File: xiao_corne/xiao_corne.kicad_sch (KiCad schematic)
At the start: 70 parts, among them SW1 SW_Push, SW10 SW_Push, SW11 SW_Push, SW12 SW_Push, SW13 SW_Push, SW17 SW_Push, SW18 SW_Push, SW19 SW_Push, SW2 SW_Push, SW20 SW_Push, SW21 SW_Push, SW22 SW_Push, SW23 SW_Push, SW24 SW_Push, SW25 SW_Push, SW26 SW_Push, SW27 SW_Push, SW3 SW_Push, SW4 SW_Push, SW5 SW_Push, SW9 SW_Push, U1 XIAO-ESP32-S3-SMD, U2 SN74AHCT125DR, U3 MCP1253-33X50I/MS

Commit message: Hardware V0.2
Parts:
- added BT2: Battery, ScottoKeebs_Scotto:Battery, symbol Device:Battery
- added C4, C5: 10uF, footprints_grm:G-21_MUR, symbol 2025-03-05_20-15-47:GRM21BR61C106KE15K
- added C6: 1uF, footprints_cl1:CAP_CL10_SAM, symbol 2025-03-05_20-11-15:CL10B105KA8NNNC
- added D43, D44, D45, D46, D47, D48, D49, D50, D51, D52, D53, D54, D55, D56, D57, D58, D59, D60, D61, D62, D63: D, ScottoKeebs_Components:Diode_SOD-123, symbol Device:D
- added D64, D65, D66, D67, D68, D69, D70, D71, D72, D73, D74, D75, D76, D77, D78, D79, D80, D81, D82, D83, D84: LED_SK6812MINI, ScottoKeebs_Components:LED_SK6812MINI, symbol ScottoKeebs:LED_SK6812MINI
- added J1, J2: Conn_01x04_Socket, Connector_PinHeader_2.54mm:PinHeader_1x04_P2.54mm_Vertical, symbol Connector:Conn_01x04_Socket
- added SW14, SW15, SW16, SW28, SW29, SW30, SW31, SW32, SW33, SW34, SW35, SW36, SW37, SW38, SW39, SW40, SW41, SW42, SW6, SW7, SW8: SW_Push, ScottoKeebs_Hotswap:Hotswap_Choc_V1V2_1.00u, symbol Switch:SW_Push
- added U4: XIAO-ESP32-S3-SMD, Seeed_Studio_XIAO_Series:XIAO-ESP32-S3-SMD, symbol Seeed_Studio_XIAO_Series-20240814:XIAO-ESP32-S3-SMD
- added U5: MCP1253-33X50I/MS, footprints_mcp:MSOP8_MC_MCH, symbol 2025-03-05_20-04-50:MCP1253-33X50I_MS
- added U6: SN74AHCT125DR, footprints_sn7:D14, symbol 2025-03-05_20-42-17:SN74AHCT125DR
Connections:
- net +5V: now also C4.1, D64.1 (VDD), D65.1 (VDD), D66.1 (VDD), D67.1 (VDD), D68.1 (VDD), D69.1 (VDD), D70.1 (VDD), D71.1 (VDD), D72.1 (VDD), D73.1 (VDD), D74.1 (VDD), D75.1 (VDD), D76.1 (VDD), D77.1 (VDD), D78.1 (VDD), D79.1 (VDD), D80.1 (VDD), D81.1 (VDD), D82.1 (VDD), D83.1 (VDD), D84.1 (VDD), U5.2 (VOUT), U6.14 (VCC); no longer C3.1, D14.1 (VDD), D15.1 (VDD), D16.1 (VDD), D28.1 (VDD), D29.1 (VDD), D30.1 (VDD), D31.1 (VDD), D32.1 (VDD), D33.1 (VDD), D34.1 (VDD), D35.1 (VDD), D36.1 (VDD), D37.1 (VDD), D38.1 (VDD), D39.1 (VDD), D40.1 (VDD), D41.1 (VDD), D42.1 (VDD), D6.1 (VDD), D7.1 (VDD), D8.1 (VDD), U2.14 (VCC), U3.2 (VOUT)
- net C1: now also D43.2 (A), D44.2 (A), D45.2 (A), D46.2 (A), D47.2 (A), U4.6 (PA9_A5_D5_SCL); no longer D1.2 (A), D17.2 (A), D22.2 (A), D27.2 (A), D9.2 (A), U1.6 (PA9_A5_D5_SCL)
- net C2: now also D48.2 (A), D49.2 (A), D50.2 (A), D51.2 (A), U4.7 (PB08_A6_D6_TX); no longer D10.2 (A), D18.2 (A), D2.2 (A), D23.2 (A), U1.7 (PB08_A6_D6_TX)
- net C3: now also D52.2 (A), D53.2 (A), D54.2 (A), D55.2 (A), U4.8 (PB09_A7_D7_RX); no longer D11.2 (A), D19.2 (A), D24.2 (A), D3.2 (A), U1.8 (PB09_A7_D7_RX)
- net C4: now also D56.2 (A), D57.2 (A), D58.2 (A), D59.2 (A), U4.9 (PA7_A8_D8_SCK); no longer D12.2 (A), D20.2 (A), D25.2 (A), D4.2 (A), U1.9 (PA7_A8_D8_SCK)
- net C5: now also D60.2 (A), D61.2 (A), D62.2 (A), D63.2 (A), U4.10 (PA5_A9_D9_MISO); no longer D13.2 (A), D21.2 (A), D26.2 (A), D5.2 (A), U1.10 (PA5_A9_D9_MISO)
- net GND: now also BT2.2 (-), C4.2, C5.2, D64.3 (VSS), D65.3 (VSS), D66.3 (VSS), D67.3 (VSS), D68.3 (VSS), D69.3 (VSS), D70.3 (VSS), D71.3 (VSS), D72.3 (VSS), D73.3 (VSS), D74.3 (VSS), D75.3 (VSS), D76.3 (VSS), D77.3 (VSS), D78.3 (VSS), D79.3 (VSS), D80.3 (VSS), D81.3 (VSS), D82.3 (VSS), D83.3 (VSS), D84.3 (VSS), J2.4 (Pin_4), U4.13 (GND), U4.16 (GND), U4.20 (GND), U5.4 (GND), U5.8 (SELECT), U6.1 (*1OE), U6.7 (GND); no longer BT1.2 (-), C2.2, C3.2, D14.3 (VSS), D15.3 (VSS), D16.3 (VSS), D28.3 (VSS), D29.3 (VSS), D30.3 (VSS), D31.3 (VSS), D32.3 (VSS), D33.3 (VSS), D34.3 (VSS), D35.3 (VSS), D36.3 (VSS), D37.3 (VSS), D38.3 (VSS), D39.3 (VSS), D40.3 (VSS), D41.3 (VSS), D42.3 (VSS), D6.3 (VSS), D7.3 (VSS), D8.3 (VSS), U1.13 (GND), U1.16 (GND), U1.20 (GND), U2.1 (*1OE), U2.7 (GND), U3.4 (GND), U3.8 (SELECT)
- net LED_3v: now also U4.11 (PA6_A10_D10_MOSI), U6.2 (1A); no longer U1.11 (PA6_A10_D10_MOSI), U2.2 (1A)
- net LED_5v: now also D64.4 (DIN), U6.3 (1Y); no longer D6.4 (DIN), U2.3 (1Y)
- net R1: now also SW35.2, SW39.2, SW6.2, SW7.2, SW8.2, U4.1 (PA02_A0_D0); no longer SW1.2, SW2.2, SW3.2, SW4.2, SW5.2, U1.1 (PA02_A0_D0)
- net R2: now also SW14.2, SW15.2, SW16.2, SW36.2, SW40.2, U4.2 (PA4_A1_D1); no longer SW10.2, SW11.2, SW12.2, SW13.2, SW9.2, U1.2 (PA4_A1_D1)
- net R3: now also SW28.2, SW31.2, SW33.2, SW37.2, SW41.2, U4.3 (PA10_A2_D2); no longer SW17.2, SW18.2, SW19.2, SW20.2, SW21.2, U1.3 (PA10_A2_D2)
- net R4: now also SW29.2, SW32.2, SW34.2, SW38.2, SW42.2, U4.4 (PA11_A3_D3); no longer SW22.2, SW23.2, SW24.2, SW25.2, SW26.2, U1.4 (PA11_A3_D3)
- net R5: now also SW30.2, U4.5 (PA8_A4_D4_SDA); no longer SW27.2, U1.5 (PA8_A4_D4_SDA)
- net +5V L USB: now reaches U1.14 (5V)
- net +5V L USB: now also J1.1 (Pin_1)
- new net: D60.1 (K), SW39.1
- new net: D66.4 (DIN), D84.2 (DOUT)
- new net: D82.2 (DOUT), D84.4 (DIN)
- new net: C5.1, U4.12 (3V3), U5.3 (VIN), U5.7 (*SHDN)
- new net: C6.1, U5.6 (C+)
- new net: C6.2, U5.5 (C-)
- new net: D50.1 (K), SW31.1
- new net: D59.1 (K), SW38.1
- new net: BT2.1 (+), U4.15 (BAT)
- new net: D46.1 (K), SW29.1
- new net: D75.2 (DOUT), D78.4 (DIN)
- new net: D43.1 (K), SW6.1
- new net: D53.1 (K), SW16.1
- new net: D63.1 (K), SW42.1
- new net: D48.1 (K), SW7.1
- new net: D62.1 (K), SW41.1
- new net: D66.2 (DOUT), D69.4 (DIN)
- new net: D61.1 (K), SW40.1
- new net: D76.2 (DOUT), D79.4 (DIN)
- new net: D73.2 (DOUT), D76.4 (DIN)
- new net: D49.1 (K), SW15.1
- new net: D80.2 (DOUT), D82.4 (DIN)
- new net: D77.2 (DOUT), D80.4 (DIN)
- new net: D51.1 (K), SW32.1
- new net: D54.1 (K), SW33.1
- new net: D79.2 (DOUT), D81.4 (DIN)
- new net: D68.2 (DOUT), D71.4 (DIN)
- new net: D65.2 (DOUT), D68.4 (DIN)
- new net: D56.1 (K), SW35.1
- new net: D45.1 (K), SW28.1
- new net: D44.1 (K), SW14.1
- new net: D65.4 (DIN), D83.2 (DOUT)
- new net: D71.2 (DOUT), D74.4 (DIN)
- new net: D69.2 (DOUT), D72.4 (DIN)
- new net: D52.1 (K), SW8.1
- new net: D64.2 (DOUT), D67.4 (DIN)
- new net: D74.2 (DOUT), D77.4 (DIN)
- new net: D47.1 (K), SW30.1
- new net: D55.1 (K), SW34.1
- new net: D67.2 (DOUT), D70.4 (DIN)
- new net: D70.2 (DOUT), D73.4 (DIN)
- new net: D81.2 (DOUT), D83.4 (DIN)
- new net: D57.1 (K), SW36.1
- new net: D72.2 (DOUT), D75.4 (DIN)
- new net: D58.1 (K), SW37.1
- new net +5V L: C3.1, D14.1 (VDD), D15.1 (VDD), D16.1 (VDD), D28.1 (VDD), D29.1 (VDD), D30.1 (VDD), D31.1 (VDD), D32.1 (VDD), D33.1 (VDD), D34.1 (VDD), D35.1 (VDD), D36.1 (VDD), D37.1 (VDD), D38.1 (VDD), D39.1 (VDD), D40.1 (VDD), D41.1 (VDD), D42.1 (VDD), D6.1 (VDD), D7.1 (VDD), D8.1 (VDD), U2.14 (VCC), U3.2 (VOUT)
- new net +5V USB: J2.1 (Pin_1), U4.14 (5V)
- new net C1 L: D1.2 (A), D17.2 (A), D22.2 (A), D27.2 (A), D9.2 (A), U1.6 (PA9_A5_D5_SCL)
- new net C2 L: D10.2 (A), D18.2 (A), D2.2 (A), D23.2 (A), U1.7 (PB08_A6_D6_TX)
- new net C3 L: D11.2 (A), D19.2 (A), D24.2 (A), D3.2 (A), U1.8 (PB09_A7_D7_RX)
- new net C4 L: D12.2 (A), D20.2 (A), D25.2 (A), D4.2 (A), U1.9 (PA7_A8_D8_SCK)
- new net C5 L: D13.2 (A), D21.2 (A), D26.2 (A), D5.2 (A), U1.10 (PA5_A9_D9_MISO)
- new net GND L: BT1.2 (-), C2.2, C3.2, D14.3 (VSS), D15.3 (VSS), D16.3 (VSS), D28.3 (VSS), D29.3 (VSS), D30.3 (VSS), D31.3 (VSS), D32.3 (VSS), D33.3 (VSS), D34.3 (VSS), D35.3 (VSS), D36.3 (VSS), D37.3 (VSS), D38.3 (VSS), D39.3 (VSS), D40.3 (VSS), D41.3 (VSS), D42.3 (VSS), D6.3 (VSS), D7.3 (VSS), D8.3 (VSS), J1.4 (Pin_4), U1.13 (GND), U1.16 (GND), U1.20 (GND), U2.1 (*1OE), U2.7 (GND), U3.4 (GND), U3.8 (SELECT)
- new net LED_3v L: U1.11 (PA6_A10_D10_MOSI), U2.2 (1A)
- new net LED_5v L: D6.4 (DIN), U2.3 (1Y)
- new net R1 L: SW1.2, SW2.2, SW3.2, SW4.2, SW5.2, U1.1 (PA02_A0_D0)
- new net R2 L: SW10.2, SW11.2, SW12.2, SW13.2, SW9.2, U1.2 (PA4_A1_D1)
- new net R3 L: SW17.2, SW18.2, SW19.2, SW20.2, SW21.2, U1.3 (PA10_A2_D2)
- new net R4 L: SW22.2, SW23.2, SW24.2, SW25.2, SW26.2, U1.4 (PA11_A3_D3)
- new net R5 L: SW27.2, U1.5 (PA8_A4_D4_SDA)
- no-connect marks 18 -> 40

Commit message: Major work for update to 0.3!
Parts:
- removed C1, C6: 1uF, footprints_cl1:CAP_CL10_SAM, symbol 2025-03-05_20-11-15:CL10B105KA8NNNC
- removed C2, C3, C4, C5: 10uF, footprints_grm:G-21_MUR, symbol 2025-03-05_20-15-47:GRM21BR61C106KE15K
- removed U1, U4: XIAO-ESP32-S3-SMD, Seeed_Studio_XIAO_Series:XIAO-ESP32-S3-SMD, symbol Seeed_Studio_XIAO_Series-20240814:XIAO-ESP32-S3-SMD
- removed U3, U5: MCP1253-33X50I/MS, footprints_mcp:MSOP8_MC_MCH, symbol 2025-03-05_20-04-50:MCP1253-33X50I_MS
- added C1, C2, C3, C4, C5, C7: 10uF, Capacitor_SMD:C_0805_2012Metric, symbol Device:C
- added C10, C9: 100nF, Capacitor_SMD:C_0805_2012Metric, symbol Device:C
- added C6, C8: 1uF, Capacitor_SMD:C_0603_1608Metric, symbol Device:C
- added D78, D79, D80, D86, D87, D88: LED_SK6812MINI, ScottoKeebs_Components:LED_SK6812MINI, symbol ScottoKeebs:LED_SK6812MINI
- added J10, J2, J3, J4, J5, J7, J8, J9: Conn_01x04_Socket, Connector_PinHeader_2.54mm:PinHeader_1x04_P2.54mm_Vertical, symbol Connector:Conn_01x04_Socket
- added L1, L2: 2.2uH, Inductor_SMD:L_0805_2012Metric, symbol Device:L
- added R1, R2, R3, R4: 100k, Resistor_SMD:R_0805_2012Metric, symbol Device:R
- added S1, S2: SLW-864574-5A-RA-N-D, KiCad:SLW8645745ARAND, symbol SLW-864574-5A-RA-N-D:SLW-864574-5A-RA-N-D
- added U3, U4: XIAO-HALF-HOLE-23P, xiao ESP32S3 Plus_PCB:MOUDLE23P-SMD-2.54-21X17.8MM.kicad_mod.kicad_sym, symbol MOUDLE-SEEEDUINO-XIAO-ESP32S3-Plus:Module/XIAO-HALF-HOLE-23P
- added U5, U6: TPS61202DRCR, TPS61202DRCR:VREG_V62_16624-01YE, symbol TPS61202DRCR:TPS61202DRCR
- renumbered D60 to D10, D9 to D11, D10 to D12, D11 to D13, D12 to D14, D13 to D15, D6 to D16, D7 to D17, D8 to D18, D14 to D19, D15 to D20, D16 to D21, D28 to D22, D29 to D23, D44 to D24, D49 to D25, D53 to D26, D57 to D27, D61 to D28, D64 to D29, D67 to D30, D70 to D31, D73 to D32, D76 to D33, D79 to D34, D81 to D35, D83 to D36, D17 to D37, D18 to D38, D19 to D39, D20 to D40, D21 to D41, D45 to D42, D50 to D43, D54 to D44, D58 to D45, D62 to D46, D30 to D47, D31 to D48, D32 to D49, D33 to D50, D34 to D51, D35 to D52, D36 to D53, D37 to D54, D65 to D55, D68 to D56, D71 to D57, D74 to D58, D77 to D59, D43 to D6, D80 to D60, D82 to D61, D84 to D62, D22 to D63, D23 to D64, D24 to D65, D25 to D66, D26 to D67, D46 to D68, D51 to D69, D48 to D7, D55 to D70, D59 to D71, D63 to D72, D38 to D73, D39 to D74, D40 to D75, D41 to D76, D42 to D77, D52 to D8, D66 to D81, D69 to D82, D72 to D83, D75 to D84, D78 to D85, D27 to D89, D56 to D9, D47 to D90, J2 to J1, J1 to J6, SW39 to SW10, SW9 to SW11, SW10 to SW12, SW11 to SW13, SW12 to SW14, SW13 to SW15, SW14 to SW16, SW15 to SW17, SW16 to SW18, SW36 to SW19, SW40 to SW20, SW17 to SW21, SW18 to SW22, SW19 to SW23, SW20 to SW24, SW21 to SW25, SW28 to SW26, SW31 to SW27, SW33 to SW28, SW37 to SW29, SW41 to SW30, SW22 to SW31, SW23 to SW32, SW24 to SW33, SW25 to SW34, SW26 to SW35, SW29 to SW36, SW32 to SW37, SW34 to SW38, SW38 to SW39, SW42 to SW40, SW27 to SW41, SW30 to SW42, SW35 to SW9, U2 to U1, U6 to U2
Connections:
- net +5V: now also C3.2, C4.2, D86.1 (VDD), D87.1 (VDD), D88.1 (VDD), J2.1 (Pin_1), J3.1 (Pin_1), U6.10 (FB), U6.2 (VOUT)
- net +5V L: now also C1.2, C2.2, D78.1 (VDD), D79.1 (VDD), D80.1 (VDD), J4.1 (Pin_1), J5.1 (Pin_1), U5.10 (FB), U5.2 (VOUT)
- net +5V L USB: now also U3.14 (VBUS)
- net +5V USB: now also U4.14 (VBUS)
- net C1: now also U4.6 (GPIO6_D5/A5/I2C_SCL)
- net C1 L: now also U3.6 (GPIO6_D5/A5/I2C_SCL)
- net C2: now also U4.7 (U0TXD_D6/TX)
- net C2 L: now also U3.7 (U0TXD_D6/TX)
- net C3: now also U4.8 (U0RXD_D7/RX)
- net C3 L: now also U3.8 (U0RXD_D7/RX)
- net C4: now also U4.9 (GPIO7_D8/A8/SCK)
- net C4 L: now also U3.9 (GPIO7_D8/A8/SCK)
- net C5: now also U4.10 (GPIO8_D9/A9/MISO)
- net C5 L: now also U3.10 (GPIO8_D9/A9/MISO)
- net GND: now also C10.1, C3.1, C4.1, C7.1, C8.1, D86.3 (VSS), D87.3 (VSS), D88.3 (VSS), J2.4 (Pin_4), J3.4 (Pin_4), J7.4 (Pin_4), J8.4 (Pin_4), U4.13 (GND), U4.26 (GND), U4.32 (BAT-), U6.4 (PGND), U6.9 (GND)
- net GND L: now also C1.1, C2.1, C5.1, C6.1, C9.1, D78.3 (VSS), D79.3 (VSS), D80.3 (VSS), J10.4 (Pin_4), J4.4 (Pin_4), J5.4 (Pin_4), J9.4 (Pin_4), U3.13 (GND), U3.26 (GND), U3.32 (BAT-), U5.4 (PGND), U5.9 (GND)
- net LED_3v: now also U4.11 (GPIO9_D10/A10/MOSI)
- net LED_3v L: now also U3.11 (GPIO9_D10/A10/MOSI)
- net R1: now also U4.1 (GPIO1_D0/A0)
- net R1 L: now also U3.1 (GPIO1_D0/A0)
- net R2: now also U4.2 (GPIO2_D1/A1)
- net R2 L: now also U3.2 (GPIO2_D1/A1)
- net R3: now also U4.3 (GPIO3_D2/A2)
- net R3 L: now also U3.3 (GPIO3_D2/A2)
- net R4: now also U4.4 (GPIO4_D3/A3)
- net R4 L: now also U3.4 (GPIO4_D3/A3)
- net R5: now also U4.5 (GPIO5_D4/A4/I2C_SDA)
- net R5 L: now also U3.5 (GPIO5_D4/A4/I2C_SDA)
- net at BT2.1 (+): now also S2.3
- net at D85.2 (DOUT): now also D86.4 (DIN)
- net at D77.2 (DOUT): now also D78.4 (DIN)
- net at BT1.1 (+): now also S1.3
- new net: R1.2, U3.20 (GPIO10_XMCLK/ADC_BAT)
- new net: R3.2, S1.2, U3.33 (BAT+)
- new net: C6.2, U5.1 (VAUX)
- new net: R4.2, S2.2, U4.33 (BAT+)
- new net: C9.2, R1.1, R3.1
- new net: L1.1, U5.3 (L)
- new net: D87.2 (DOUT), D88.4 (DIN)
- new net: D79.2 (DOUT), D80.4 (DIN)
- new net: L2.1, U6.3 (L)
- new net: D86.2 (DOUT), D87.4 (DIN)
- new net: D78.2 (DOUT), D79.4 (DIN)
- new net: C10.2, R2.1, R4.1
- new net: R2.2, U4.20 (GPIO10_XMCLK/ADC_BAT)
- new net +3.3V: C7.2, C8.2, J7.1 (Pin_1), J8.1 (Pin_1), L2.2, U4.12 (VCC_3V3), U6.1 (VAUX), U6.5 (VIN), U6.6 (EN), U6.7 (UVLO), U6.8 (PS)
- new net +3.3V L: C5.2, J10.1 (Pin_1), J9.1 (Pin_1), L1.2, U3.12 (VCC_3V3), U5.5 (VIN), U5.6 (EN), U5.7 (UVLO), U5.8 (PS)
- new net GPIO_1: J2.2 (Pin_2), U4.15 (GPIO38_DVP_VSYNC/I2S_SD)
- new net GPIO_1_L: J4.2 (Pin_2), U3.15 (GPIO38_DVP_VSYNC/I2S_SD)
- new net GPIO_2: J2.3 (Pin_3), U4.16 (GPIO39_CAM_SCL/I2S_SCK)
- new net GPIO_2_L: J4.3 (Pin_3), U3.16 (GPIO39_CAM_SCL/I2S_SCK)
- new net GPIO_3: J7.2 (Pin_2), U4.17 (GPIO40_CAM_SDA/I2S_WS)
- new net GPIO_3_L: J9.2 (Pin_2), U3.17 (GPIO40_CAM_SDA/I2S_WS)
- new net GPIO_4: J7.3 (Pin_3), U4.18 (GPIO41_PDM_DATA/RX1)
- new net GPIO_4_L: J9.3 (Pin_3), U3.18 (GPIO41_PDM_DATA/RX1)
- new net GPIO_5: J3.2 (Pin_2), U4.19 (GPIO42_PDM_CLK/TX1)
- new net GPIO_5_L: J5.2 (Pin_2), U3.19 (GPIO42_PDM_CLK/TX1)
- new net GPIO_6: J3.3 (Pin_3), U4.21 (GPIO11_DVP_Y8/SPI_MOSI1)
- new net GPIO_6_L: J5.3 (Pin_3), U3.21 (GPIO11_DVP_Y8/SPI_MOSI1)
- new net GPIO_7: J8.2 (Pin_2), U4.22 (GPIO12_DVP_Y7/SPI_MISO1)
- new net GPIO_7_L: J10.2 (Pin_2), U3.22 (GPIO12_DVP_Y7/SPI_MISO1)
- new net GPIO_8: J8.3 (Pin_3), U4.23 (GPIO13_DVP_PCLK/SPI_SCK1)
- new net GPIO_8_L: J10.3 (Pin_3), U3.23 (GPIO13_DVP_PCLK/SPI_SCK1)
- no-connect marks 40 -> 46
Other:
- note added: "Done (v0.2 - v0.3): Add new LEDs Change voltage converter Switch to esp32c3 plus Add battery voltage sense line Expansion board GPIO Add switch for battery"
- moved on the sheet: J1

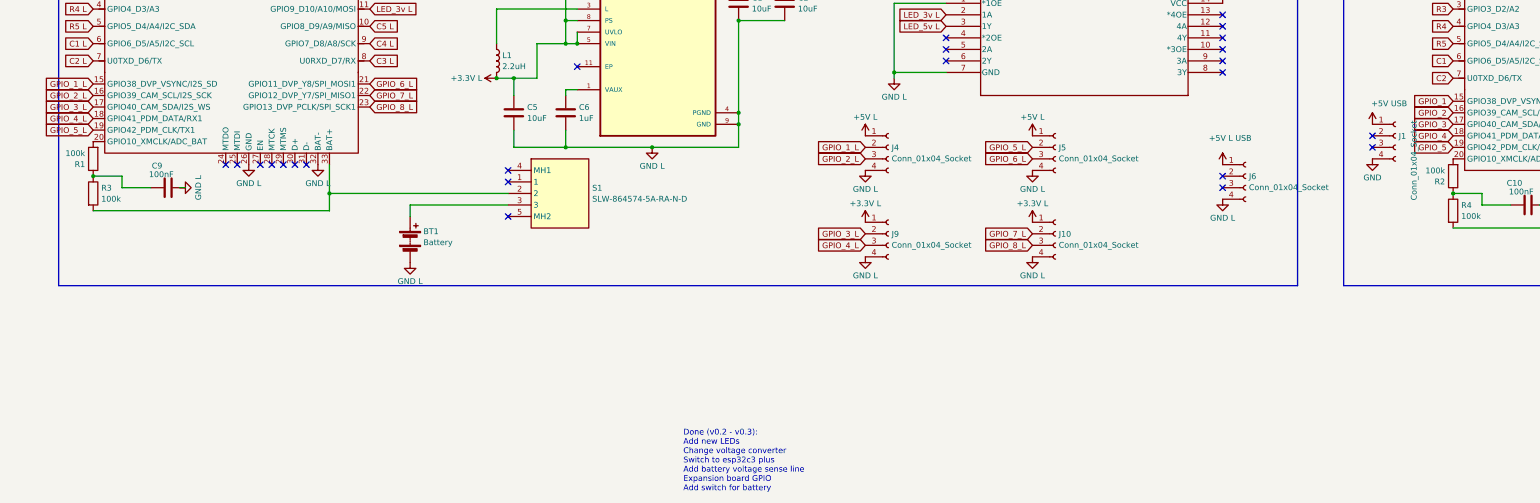
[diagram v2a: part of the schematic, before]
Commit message: Fixed issue with battery voltage monitor
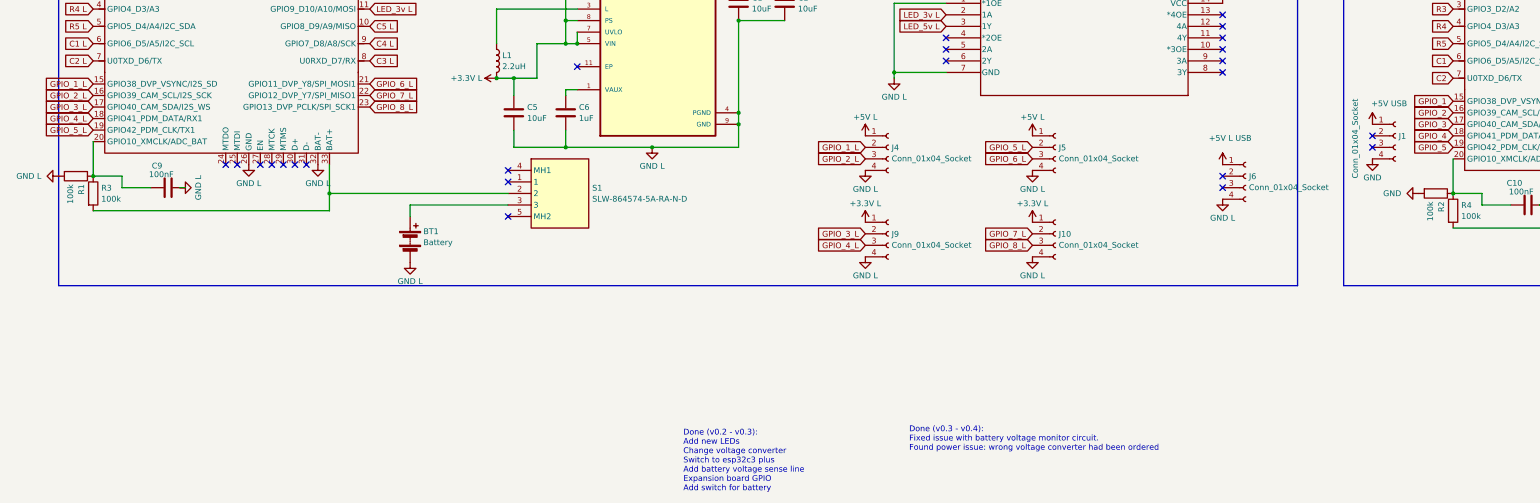
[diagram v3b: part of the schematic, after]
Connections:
- net GND: now also R2.2
- net GND L: now also R1.2
- net at U3.20 (GPIO10_XMCLK/ADC_BAT): now also C9.2, R1.1, R3.1; no longer R1.2
- net at C10.2, R2.1, R4.1: now also U4.20 (GPIO10_XMCLK/ADC_BAT)
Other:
- note added: "Done (v0.3 - v0.4): Fixed issue with battery voltage monitor circuit. Found power issue: wrong voltage converter had been ordered"
- moved on the sheet: R1, R2
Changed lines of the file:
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@@
 		)
 	)
+	(text "Done (v0.3 - v0.4):\nFixed issue with battery voltage monitor circuit.\nFound power issue: wrong voltage converter had been ordered"
+		(exclude_from_sim no)
+		(at 201.422 226.822 0)
+		(effects
+			(font
+				(size 1.27 1.27)
+			)
+			(justify left)
+		)
+	)
 	(junction
 		(at 527.05 109.22)
@@
 	)
 	(junction
+		(at 321.31 172.72)
+		(diameter 0)
+		(color 0 0 0 0)
+	)
+	(junction
 		(at 408.94 148.59)
 		(diameter 0)
@@
 	)
 	(junction
+		(at 21.59 168.91)
+		(diameter 0)
+		(color 0 0 0 0)
+	)
+	(junction
 		(at 213.36 54.61)
 		(diameter 0)
@@
 	)
 	(junction
-		(at 21.59 168.91)
-		(diameter 0)
-		(color 0 0 0 0)
-	)
-	(junction
 		(at 44.45 27.94)
 		(diameter 0)
@@
 	)
 	(junction
-		(at 321.31 172.72)
-		(diameter 0)
-		(color 0 0 0 0)
-	)
-	(junction
 		(at 228.6 39.37)
 		(diameter 0)
@@
 	(wire
 		(pts
+			(xy 321.31 165.1) (xy 321.31 172.72)
+		)
+		(stroke
+			(width 0)
+			(type default)
+		)
+	)
+	(wire
+		(pts
 			(xy 182.88 54.61) (xy 167.64 54.61)
 		)
@@
 	(wire
 		(pts
+			(xy 21.59 161.29) (xy 21.59 168.91)
+		)
+		(stroke
+			(width 0)
+			(type default)
+		)
+	)
+	(wire
+		(pts
 			(xy 511.81 39.37) (xy 496.57 39.37)
 		)
@@
 	)
 	(symbol
+		(lib_id "power:GND")
+		(at 13.97 168.91 270)
+		(unit 1)
+		(exclude_from_sim no)
+		(in_bom yes)
+		(on_board yes)
+		(dnp no)
+		(fields_autoplaced yes)
+		(property "Reference" "#PWR049"
+			(at 7.62 168.91 0)
+			(effects
+				(font
+					(size 1.27 1.27)
+				)
+				(hide yes)
+			)
+		)
+		(property "Value" "GND L"
+			(at 10.16 168.9099 90)
+			(effects
+				(font
+					(size 1.27 1.27)
+				)
+				(justify right)
+			)
+		)
+		(property "Footprint" ""
+			(at 13.97 168.91 0)
+			(effects
+				(font
+					(size 1.27 1.27)
+				)
+				(hide yes)
+			)
+		)
+		(property "Datasheet" ""
+			(at 13.97 168.91 0)
+			(effects
+				(font
+					(size 1.27 1.27)
+				)
+				(hide yes)
+			)
+		)
+		(property "Description" "Power symbol creates a global label with name \"GND\" , ground"
+			(at 13.97 168.91 0)
+			(effects
+				(font
+					(size 1.27 1.27)
+				)
+				(hide yes)
+			)
+		)
+		(pin "1"
+		)
+		(instances
+			(project "xiao_corne"
+				(path "/efa30048-eef2-4d23-8f91-f1f3cca8359e"
+					(reference "#PWR049")
+					(unit 1)
+				)
+			)
+		)
+	)
+	(symbol
 		(lib_id "ScottoKeebs:LED_SK6812MINI")
 		(at 527.05 74.93 0)
@@
 	(symbol
 		(lib_id "Device:R")
-		(at 21.59 165.1 180)
+		(at 17.78 168.91 270)
 		(unit 1)
 		(exclude_from_sim no)
@@
 		(dnp no)
 		(property "Reference" "R1"
-			(at 19.812 166.3122 0)
+			(at 18.9922 170.688 0)
 			(effects
 				(font
@@
 		)
 		(property "Value" "100k"
-			(at 19.812 163.8879 0)
+			(at 16.5679 170.688 0)
 			(effects
 				(font
@@
 		)
 		(property "Footprint" "Resistor_SMD:R_0805_2012Metric"
-			(at 23.368 165.1 90)
+			(at 17.78 167.132 90)
 			(effects
 				(font
@@
 		)
 		(property "Datasheet" "~"
-			(at 21.59 165.1 0)
+			(at 17.78 168.91 0)
 			(effects
 				(font
@@
 		)
 		(property "Description" "Resistor"
-			(at 21.59 165.1 0)
+			(at 17.78 168.91 0)
 			(effects
 				(font
@@
 	)
 	(symbol
+		(lib_id "power:GND")
+		(at 313.69 172.72 270)
+		(unit 1)
+		(exclude_from_sim no)
+		(in_bom yes)
+		(on_board yes)
+		(dnp no)
+		(fields_autoplaced yes)
+		(property "Reference" "#PWR050"
+			(at 307.34 172.72 0)
+			(effects
+				(font
+					(size 1.27 1.27)
+				)
+				(hide yes)
+			)
+		)
+		(property "Value" "GND"
+			(at 309.88 172.7199 90)
+			(effects
+				(font
+					(size 1.27 1.27)
+				)
+				(justify right)
+			)
+		)
+		(property "Footprint" ""
+			(at 313.69 172.72 0)
+			(effects
+				(font
+					(size 1.27 1.27)
+				)
+				(hide yes)
+			)
+		)
+		(property "Datasheet" ""
+			(at 313.69 172.72 0)
+			(effects
+				(font
+					(size 1.27 1.27)
+				)
+				(hide yes)
+			)
+		)
+		(property "Description" "Power symbol creates a global label with name \"GND\" , ground"
+			(at 313.69 172.72 0)
+			(effects
+				(font
+					(size 1.27 1.27)
+				)
+				(hide yes)
+			)
+		)
+		(pin "1"
+		)
+		(instances
+			(project "xiao_corne"
+				(path "/efa30048-eef2-4d23-8f91-f1f3cca8359e"
+					(reference "#PWR050")
+					(unit 1)
+				)
+			)
+		)
+	)
+	(symbol
 		(lib_id "ScottoKeebs:LED_SK6812MINI")
 		(at 228.6 101.6 0)
@@
 		)
 		(property "Value" "Conn_01x04_Socket"
-			(at 312.674 174.244 90)
+			(at 299.72 169.418 90)
 			(effects
 				(font
@@
 	(symbol
 		(lib_id "Device:R")
-		(at 321.31 168.91 180)
+		(at 317.5 172.72 270)
 		(unit 1)
 		(exclude_from_sim no)
@@
 		(dnp no)
 		(property "Reference" "R2"
-			(at 319.532 170.1222 0)
+			(at 318.7122 174.498 0)
 			(effects
 				(font
@@
 		)
 		(property "Value" "100k"
-			(at 319.532 167.6979 0)
+			(at 316.2879 174.498 0)
 			(effects
 				(font
@@
 		)
 		(property "Footprint" "Resistor_SMD:R_0805_2012Metric"
-			(at 323.088 168.91 90)
+			(at 317.5 170.942 90)
 			(effects
 				(font
@@
 		)
 		(property "Datasheet" "~"
-			(at 321.31 168.91 0)
+			(at 317.5 172.72 0)
 			(effects
 				(font
@@
 		)
 		(property "Description" "Resistor"
-			(at 321.31 168.91 0)
+			(at 317.5 172.72 0)
 			(effects
 				(font
